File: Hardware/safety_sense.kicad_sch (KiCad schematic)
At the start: 21 parts, among them U11 FODM217B, U12 TLP291-4, U13 TLP291-4

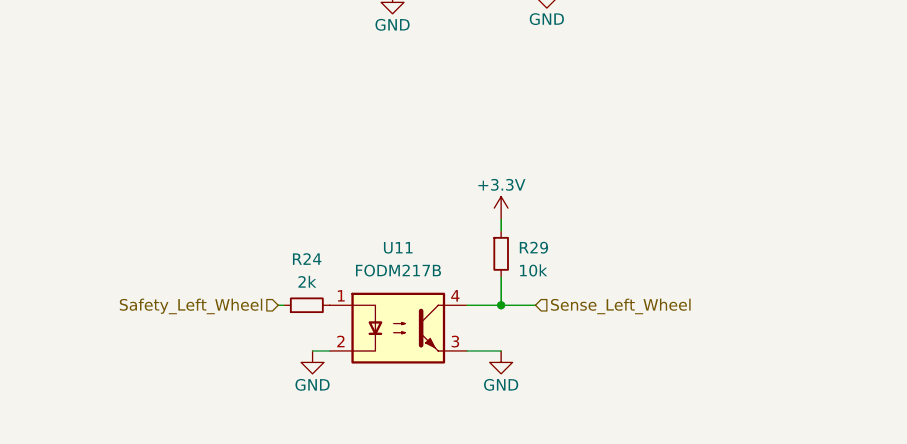
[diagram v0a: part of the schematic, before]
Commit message: Changes in current layout, added tensometers to layout
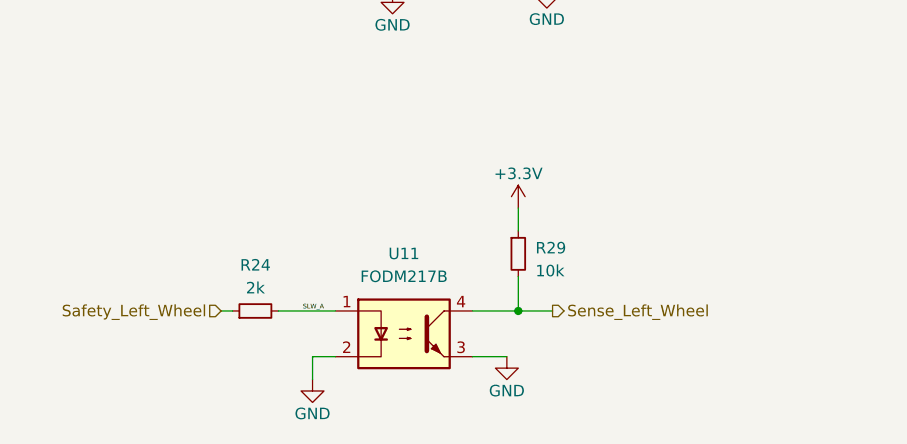
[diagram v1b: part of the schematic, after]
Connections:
- net SLW_A: now reaches R24.2, U11.1
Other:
- moved on the sheet: R24, R29, U11
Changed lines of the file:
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@@
 	)
 	(junction
-		(at 121.285 175.895)
+		(at 123.19 176.53)
 		(diameter 0)
 		(color 0 0 0 0)
@@
 	(wire
 		(pts
+			(xy 96.52 176.53) (xy 102.87 176.53)
+		)
+		(stroke
+			(width 0)
+			(type default)
+		)
+	)
+	(wire
+		(pts
 			(xy 102.87 82.55) (xy 103.505 82.55)
 		)
@@
 	(wire
 		(pts
-			(xy 100.33 180.975) (xy 102.235 180.975)
+			(xy 100.33 181.61) (xy 102.87 181.61)
 		)
 		(stroke
@@
 	(wire
 		(pts
-			(xy 121.285 175.895) (xy 121.285 172.72)
+			(xy 123.19 176.53) (xy 123.19 172.72)
 		)
 		(stroke
@@
 	(wire
 		(pts
-			(xy 121.285 166.37) (xy 121.285 167.64)
+			(xy 123.19 165.1) (xy 123.19 167.64)
 		)
 		(stroke
@@
 	(wire
 		(pts
-			(xy 96.52 175.895) (xy 97.155 175.895)
+			(xy 90.17 176.53) (xy 91.44 176.53)
 		)
 		(stroke
@@
 	(wire
 		(pts
-			(xy 121.285 175.895) (xy 125.095 175.895)
+			(xy 123.19 176.53) (xy 127 176.53)
 		)
 		(stroke
@@
 	(wire
 		(pts
+			(xy 100.33 181.61) (xy 100.33 184.15)
+		)
+		(stroke
+			(width 0)
+			(type default)
+		)
+	)
+	(wire
+		(pts
 			(xy 177.8 114.3) (xy 177.8 113.03)
 		)
@@
 	(wire
 		(pts
-			(xy 121.285 180.975) (xy 117.475 180.975)
+			(xy 121.92 181.61) (xy 118.11 181.61)
 		)
 		(stroke
@@
 	(wire
 		(pts
-			(xy 121.285 175.895) (xy 117.475 175.895)
+			(xy 123.19 176.53) (xy 118.11 176.53)
 		)
 		(stroke
@@
 		)
 	)
+	(label "SLW_A"
+		(at 101.6 176.53 180)
+		(fields_autoplaced yes)
+		(effects
+			(font
+				(size 0.508 0.508)
+			)
+			(justify right bottom)
+		)
+	)
 	(hierarchical_label "Sens_Right_Wheel"
 		(shape output)
@@
 	(hierarchical_label "Safety_Left_Wheel"
 		(shape input)
-		(at 96.52 175.895 180)
+		(at 90.17 176.53 180)
 		(fields_autoplaced yes)
 		(effects
@@
 	)
 	(hierarchical_label "Sense_Left_Wheel"
-		(shape input)
-		(at 125.095 175.895 0)
+		(shape output)
+		(at 127 176.53 0)
 		(fields_autoplaced yes)
 		(effects
@@
 	(symbol
 		(lib_id "Device:R_Small")
-		(at 99.695 175.895 90)
+		(at 93.98 176.53 90)
 		(unit 1)
 		(exclude_from_sim no)
@@
 		(fields_autoplaced yes)
 		(property "Reference" "R24"
-			(at 99.695 170.815 90)
+			(at 93.98 171.45 90)
 			(effects
 				(font
@@
 		)
 		(property "Value" "2k"
-			(at 99.695 173.355 90)
+			(at 93.98 173.99 90)
 			(effects
 				(font
@@
 		)
 		(property "Footprint" "Resistor_SMD:R_0402_1005Metric"
-			(at 99.695 175.895 0)
+			(at 93.98 176.53 0)
 			(effects
 				(font
@@
 		)
 		(property "Datasheet" "~"
-			(at 99.695 175.895 0)
+			(at 93.98 176.53 0)
 			(effects
 				(font
@@
 		)
 		(property "Description" ""
-			(at 99.695 175.895 0)
+			(at 93.98 176.53 0)
 			(effects
 				(font
@@
 	(symbol
 		(lib_id "Device:R_Small")
-		(at 121.285 170.18 0)
+		(at 123.19 170.18 0)
 		(unit 1)
 		(exclude_from_sim no)
@@
 		(fields_autoplaced yes)
 		(property "Reference" "R29"
-			(at 123.19 169.545 0)
+			(at 125.095 169.545 0)
 			(effects
 				(font
@@
 		)
 		(property "Value" "10k"
-			(at 123.19 172.085 0)
+			(at 125.095 172.085 0)
 			(effects
 				(font
@@
 		)
 		(property "Footprint" "Resistor_SMD:R_0402_1005Metric"
-			(at 121.285 170.18 0)
+			(at 123.19 170.18 0)
 			(effects
 				(font
@@
 		)
 		(property "Datasheet" "~"
-			(at 121.285 170.18 0)
+			(at 123.19 170.18 0)
 			(effects
 				(font
@@
 		)
 		(property "Description" ""
-			(at 121.285 170.18 0)
+			(at 123.19 170.18 0)
 			(effects
 				(font
@@
 	(symbol
 		(lib_id "power:GND")
-		(at 100.33 180.975 0)
+		(at 100.33 184.15 0)
 		(unit 1)
 		(exclude_from_sim no)
@@
 		(dnp no)
 		(property "Reference" "#PWR081"
-			(at 100.33 187.325 0)
+			(at 100.33 190.5 0)
 			(effects
 				(font
@@
 		)
 		(property "Value" "GND"
-			(at 100.33 184.785 0)
+			(at 100.33 187.96 0)
 			(effects
 				(font
@@
 		)
 		(property "Footprint" ""
-			(at 100.33 180.975 0)
+			(at 100.33 184.15 0)
 			(effects
 				(font
@@
 		)
 		(property "Datasheet" ""
-			(at 100.33 180.975 0)
+			(at 100.33 184.15 0)
 			(effects
 				(font
@@
 		)
 		(property "Description" ""
-			(at 100.33 180.975 0)
+			(at 100.33 184.15 0)
 			(effects
 				(font
@@
 	(symbol
 		(lib_id "power:GND")
-		(at 121.285 180.975 0)
+		(at 121.92 181.61 0)
 		(unit 1)
 		(exclude_from_sim no)
@@
 		(dnp no)
 		(property "Reference" "#PWR087"
-			(at 121.285 187.325 0)
+			(at 121.92 187.96 0)
 			(effects
 				(font
@@
 		)
 		(property "Value" "GND"
-			(at 121.285 184.785 0)
+			(at 121.92 185.42 0)
 			(effects
 				(font
@@
 		)
 		(property "Footprint" ""
-			(at 121.285 180.975 0)
+			(at 121.92 181.61 0)
 			(effects
 				(font
@@
 		)
 		(property "Datasheet" ""
-			(at 121.285 180.975 0)
+			(at 121.92 181.61 0)
 			(effects
 				(font
@@
 		)
 		(property "Description" ""
-			(at 121.285 180.975 0)
+			(at 121.92 181.61 0)
 			(effects
 				(font
@@
 	(symbol
 		(lib_id "power:+3.3V")
-		(at 121.285 166.37 0)
+		(at 123.19 165.1 0)
 		(unit 1)
 		(exclude_from_sim no)
@@
 		(fields_autoplaced yes)
 		(property "Reference" "#PWR086"
-			(at 121.285 170.18 0)
+			(at 123.19 168.91 0)
 			(effects
 				(font
@@
 		)
 		(property "Value" "+3.3V"
-			(at 121.285 162.56 0)
+			(at 123.19 161.29 0)
 			(effects
 				(font
@@
 		)
 		(property "Footprint" ""
-			(at 121.285 166.37 0)
+			(at 123.19 165.1 0)
 			(effects
 				(font
@@
 		)
 		(property "Datasheet" ""
-			(at 121.285 166.37 0)
+			(at 123.19 165.1 0)
 			(effects
 				(font
@@
 		)
 		(property "Description" ""
-			(at 121.285 166.37 0)
+			(at 123.19 165.1 0)
 			(effects
 				(font
@@
 	(symbol
 		(lib_id "Isolator:FODM217B")
-		(at 109.855 178.435 0)
+		(at 110.49 179.07 0)
 		(unit 1)
 		(exclude_from_sim no)
@@
 		(fields_autoplaced yes)
 		(property "Reference" "U11"
-			(at 109.855 169.545 0)
+			(at 110.49 170.18 0)
 			(effects
 				(font
@@
 		)
 		(property "Value" "FODM217B"
-			(at 109.855 172.085 0)
+			(at 110.49 172.72 0)
 			(effects
 				(font
@@
 		)
 		(property "Footprint" "Package_SO:SOP-4_4.4x2.6mm_P1.27mm"
-			(at 109.855 183.515 0)
+			(at 110.49 184.15 0)
 			(effects
 				(font
@@
 		)
 		(property "Datasheet" "https://www.onsemi.com/pub/Collateral/FODM214-D.PDF"
-			(at 109.855 178.435 0)
+			(at 110.49 179.07 0)
 			(effects
 				(font
@@
 		)
 		(property "Description" ""
-			(at 109.855 178.435 0)
+			(at 110.49 179.07 0)
 			(effects
 				(font

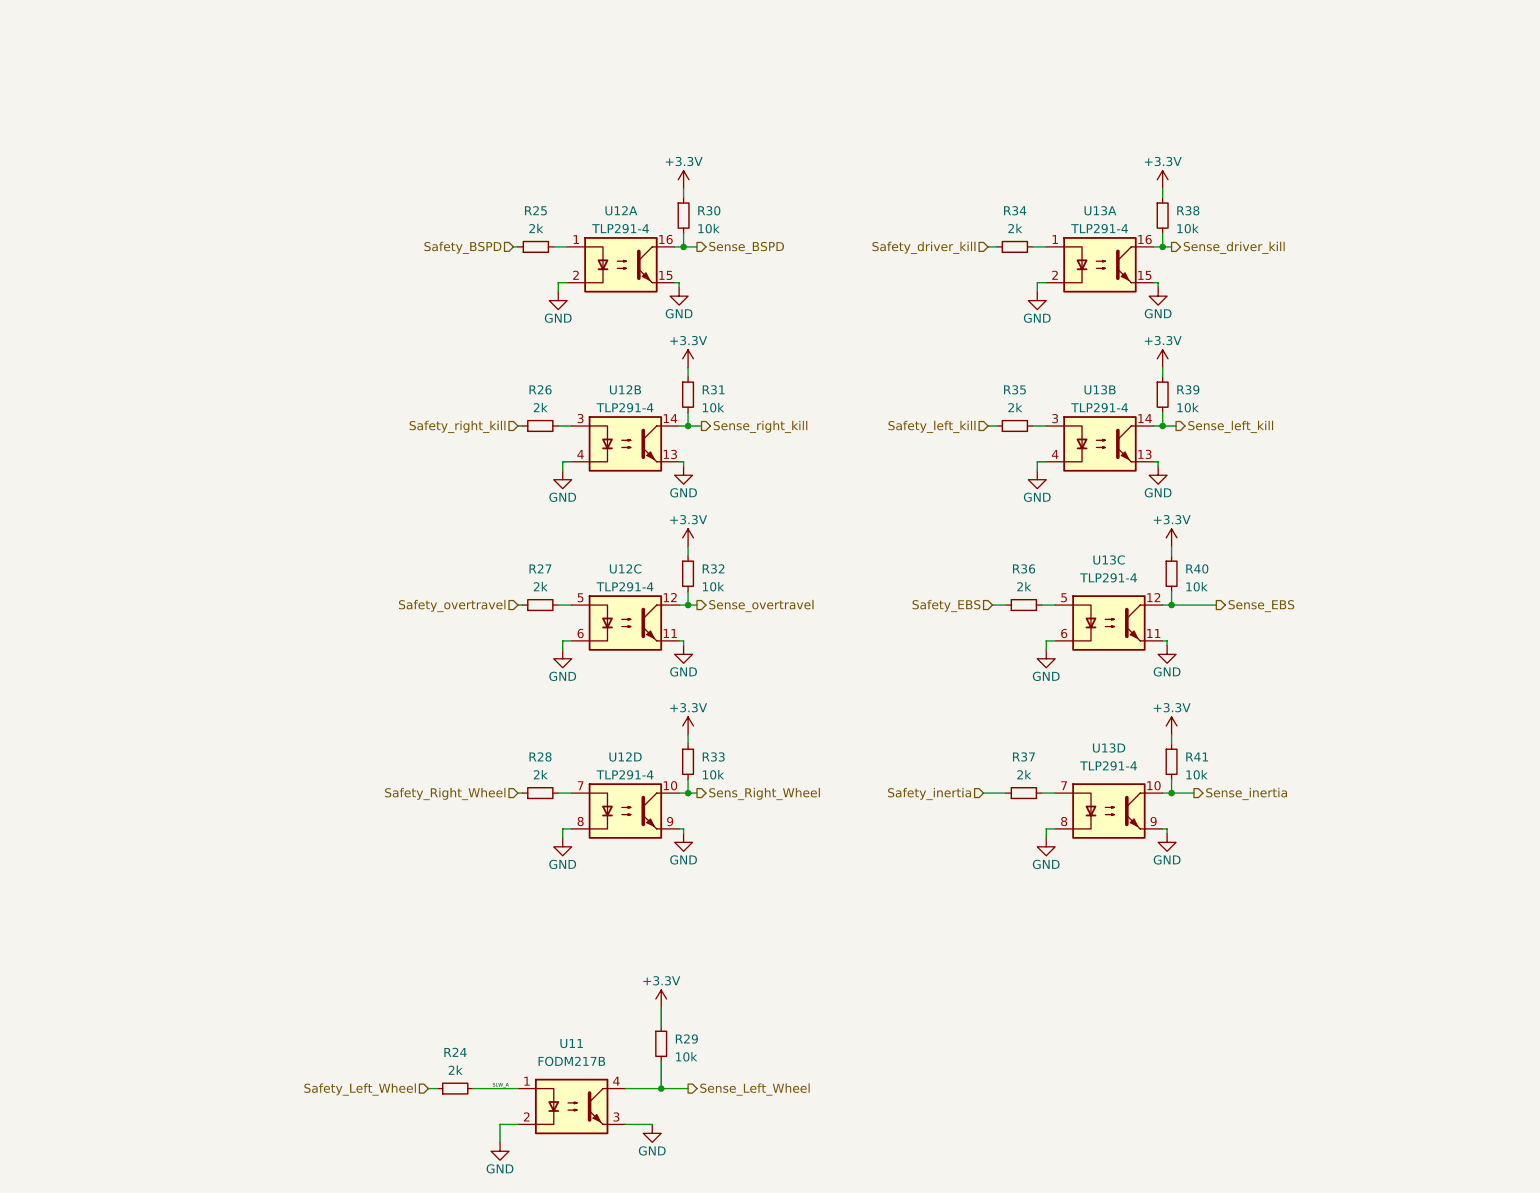
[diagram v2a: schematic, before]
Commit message: Created new hardware version 2.0
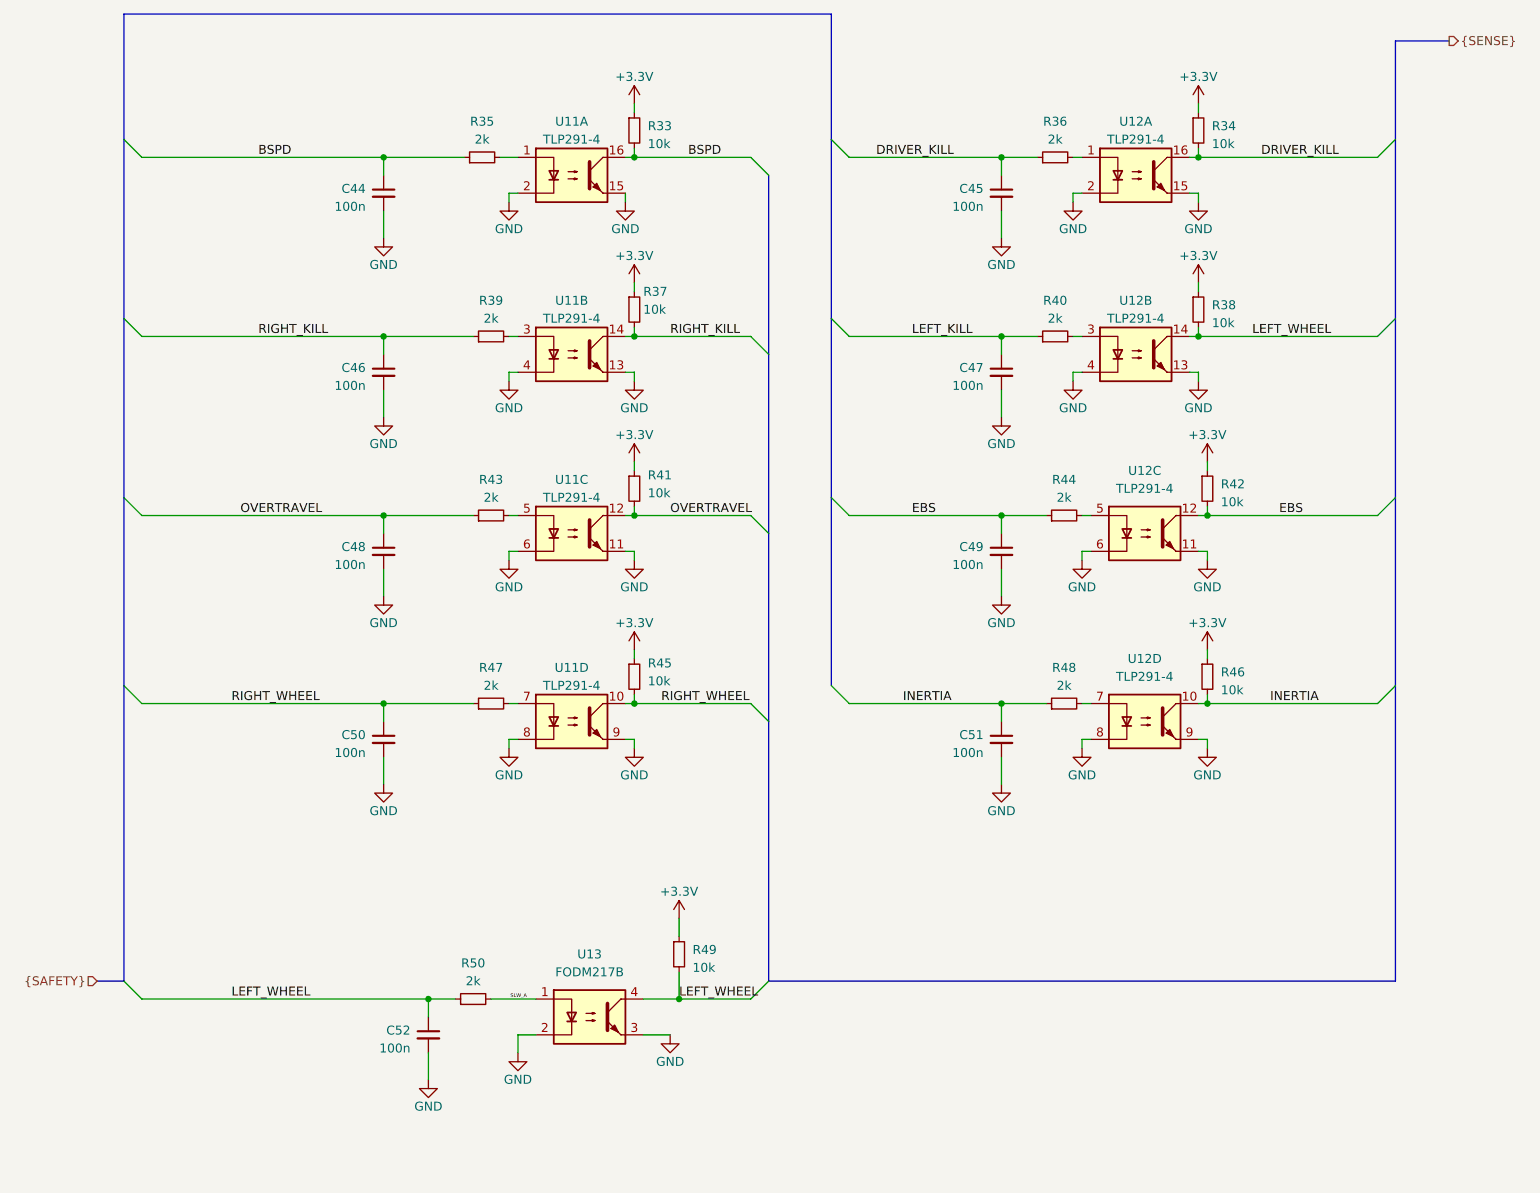
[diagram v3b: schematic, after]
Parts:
- added C44, C45, C46, C47, C48, C49, C50, C51, C52: 100n, Capacitor_SMD:C_0603_1608Metric_Pad1.08x0.95mm_HandSolder, symbol Device:C_Small
- R33: renamed from R30; footprint Resistor_SMD:R_0402_1005Metric -> Resistor_SMD:R_0603_1608Metric_Pad0.98x0.95mm_HandSolder
- R34: renamed from R38; footprint Resistor_SMD:R_0402_1005Metric -> Resistor_SMD:R_0603_1608Metric_Pad0.98x0.95mm_HandSolder
- R35: renamed from R25; footprint Resistor_SMD:R_0402_1005Metric -> Resistor_SMD:R_0603_1608Metric_Pad0.98x0.95mm_HandSolder
- R36: renamed from R34; footprint Resistor_SMD:R_0402_1005Metric -> Resistor_SMD:R_0603_1608Metric_Pad0.98x0.95mm_HandSolder
- R37: renamed from R31; footprint Resistor_SMD:R_0402_1005Metric -> Resistor_SMD:R_0603_1608Metric_Pad0.98x0.95mm_HandSolder
- R38: renamed from R39; footprint Resistor_SMD:R_0402_1005Metric -> Resistor_SMD:R_0603_1608Metric_Pad0.98x0.95mm_HandSolder
- R39: renamed from R26; footprint Resistor_SMD:R_0402_1005Metric -> Resistor_SMD:R_0603_1608Metric_Pad0.98x0.95mm_HandSolder
- R40: renamed from R35; footprint Resistor_SMD:R_0402_1005Metric -> Resistor_SMD:R_0603_1608Metric_Pad0.98x0.95mm_HandSolder
- R41: renamed from R32; footprint Resistor_SMD:R_0402_1005Metric -> Resistor_SMD:R_0603_1608Metric_Pad0.98x0.95mm_HandSolder
- R42: renamed from R40; footprint Resistor_SMD:R_0402_1005Metric -> Resistor_SMD:R_0603_1608Metric_Pad0.98x0.95mm_HandSolder
- R43: renamed from R27; footprint Resistor_SMD:R_0402_1005Metric -> Resistor_SMD:R_0603_1608Metric_Pad0.98x0.95mm_HandSolder
- R44: renamed from R36; footprint Resistor_SMD:R_0402_1005Metric -> Resistor_SMD:R_0603_1608Metric_Pad0.98x0.95mm_HandSolder
- R45: renamed from R33; footprint Resistor_SMD:R_0402_1005Metric -> Resistor_SMD:R_0603_1608Metric_Pad0.98x0.95mm_HandSolder
- R46: renamed from R41; footprint Resistor_SMD:R_0402_1005Metric -> Resistor_SMD:R_0603_1608Metric_Pad0.98x0.95mm_HandSolder
- R47: renamed from R28; footprint Resistor_SMD:R_0402_1005Metric -> Resistor_SMD:R_0603_1608Metric_Pad0.98x0.95mm_HandSolder
- R48: renamed from R37; footprint Resistor_SMD:R_0402_1005Metric -> Resistor_SMD:R_0603_1608Metric_Pad0.98x0.95mm_HandSolder
- R49: renamed from R29; footprint Resistor_SMD:R_0402_1005Metric -> Resistor_SMD:R_0603_1608Metric_Pad0.98x0.95mm_HandSolder
- R50: renamed from R24; footprint Resistor_SMD:R_0402_1005Metric -> Resistor_SMD:R_0603_1608Metric_Pad0.98x0.95mm_HandSolder
- renumbered U12 to U11, U13 to U12, U11 to U13
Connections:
- net Sens_Right_Wheel is gone; now on net RIGHT_WHEEL: R45.2, U11.10
- net Sense_BSPD is gone; now on net BSPD: R33.2, U11.16
- net Sense_EBS is gone; now on net EBS: R42.2, U12.12
- net Sense_Left_Wheel is gone; now on net LEFT_WHEEL: R49.2, U13.4
- net Sense_driver_kill is gone; now on net DRIVER_KILL: R34.2, U12.16
- net Sense_inertia is gone; now on net INERTIA: R46.2, U12.10
- net Sense_left_kill is gone; now on net LEFT_WHEEL: R38.2, U12.14
- net Sense_overtravel is gone; now on net OVERTRAVEL: R41.2, U11.12
- net Sense_right_kill is gone; now on net RIGHT_KILL: R37.2, U11.14
- net GND: now also C44.2, C45.2, C46.2, C47.2, C48.2, C49.2, C50.2, C51.2, C52.2
- net Safety_BSPD renamed BSPD
- net BSPD: now also C44.1
- net Safety_EBS renamed EBS
- net EBS: now also C49.1
- net Safety_Left_Wheel renamed LEFT_WHEEL
- net LEFT_WHEEL: now also C52.1
- net Safety_Right_Wheel renamed RIGHT_WHEEL
- net RIGHT_WHEEL: now also C50.1
- net Safety_driver_kill renamed DRIVER_KILL
- net DRIVER_KILL: now also C45.1
- net Safety_inertia renamed INERTIA
- net INERTIA: now also C51.1
- net Safety_left_kill renamed LEFT_KILL
- net LEFT_KILL: now also C47.1
- net Safety_overtravel renamed OVERTRAVEL
- net OVERTRAVEL: now also C48.1
- net Safety_right_kill renamed RIGHT_KILL
- net RIGHT_KILL: now also C46.1
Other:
- company: Author: Szymon Kostrubiec -> (none)
- title: Safety sense -> (none)
- moved on the sheet: R33, R34, R35, R36, R37, R38, R39, R40, R41, R42, R43, R44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
